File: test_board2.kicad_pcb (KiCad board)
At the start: 2 copper layers, 63.5 x 127 mm, 149 parts, among them P1 MicroB, P2 CONN_01X08, P3 CONN_01X08, P4 CONN_01X10, P5 CONN_01X06, P6 CONN_02X03, Q1 ZXMN2F30FHCT-ND, Q2 Si2305DS, SW1 SWITCH_DPDT, SW2 SW_PUSH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

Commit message: Routing complete, first check. Prior to GND fill.
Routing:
- net LED_PWR_EN: track 113.3 -> 156.0 mm, vias 4 -> 6
- net /*RESET: track 110.6 -> 132.8 mm, vias 4 -> 5
- net VCC: track 248.5 -> 259.2 mm
- net /LED_matrix/LED_3V: track 135.1 -> 144.6 mm
- net (no net): track 4.15 -> 0.00 mm
- net /MOSI: track 121.6 -> 123.2 mm
- net /LED_matrix/DIG0: track 144.0 -> 145.3 mm, vias 20 -> 19
- net I2C_SCL: track 115.4 -> 116.6 mm
- net I2C_SDA: track 97.9 -> 99.1 mm
- net /*IS_USB: track 91.1 -> 92.0 mm
- net /MISO: track 117.9 -> 118.6 mm
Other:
- board text added: "+"
- board text added: "-"

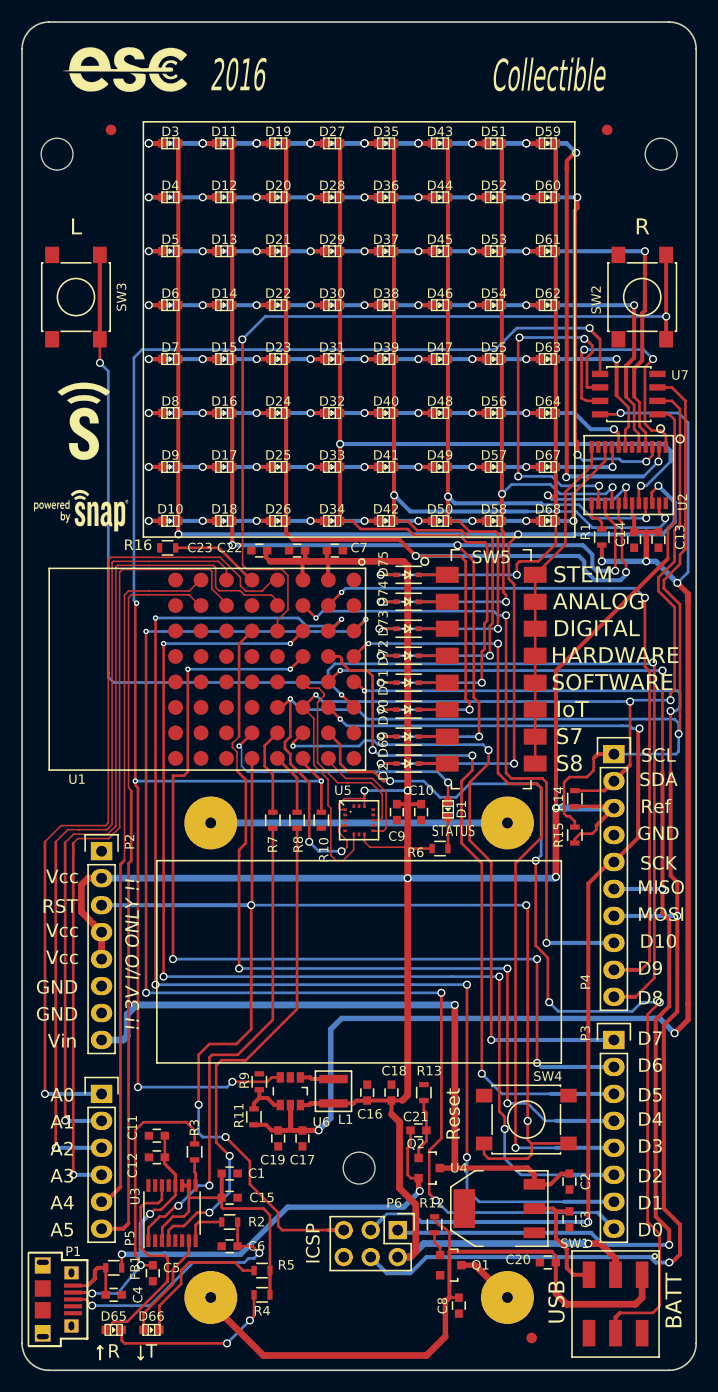
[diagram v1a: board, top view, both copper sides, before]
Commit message: Finished ground pours, all DRC passing
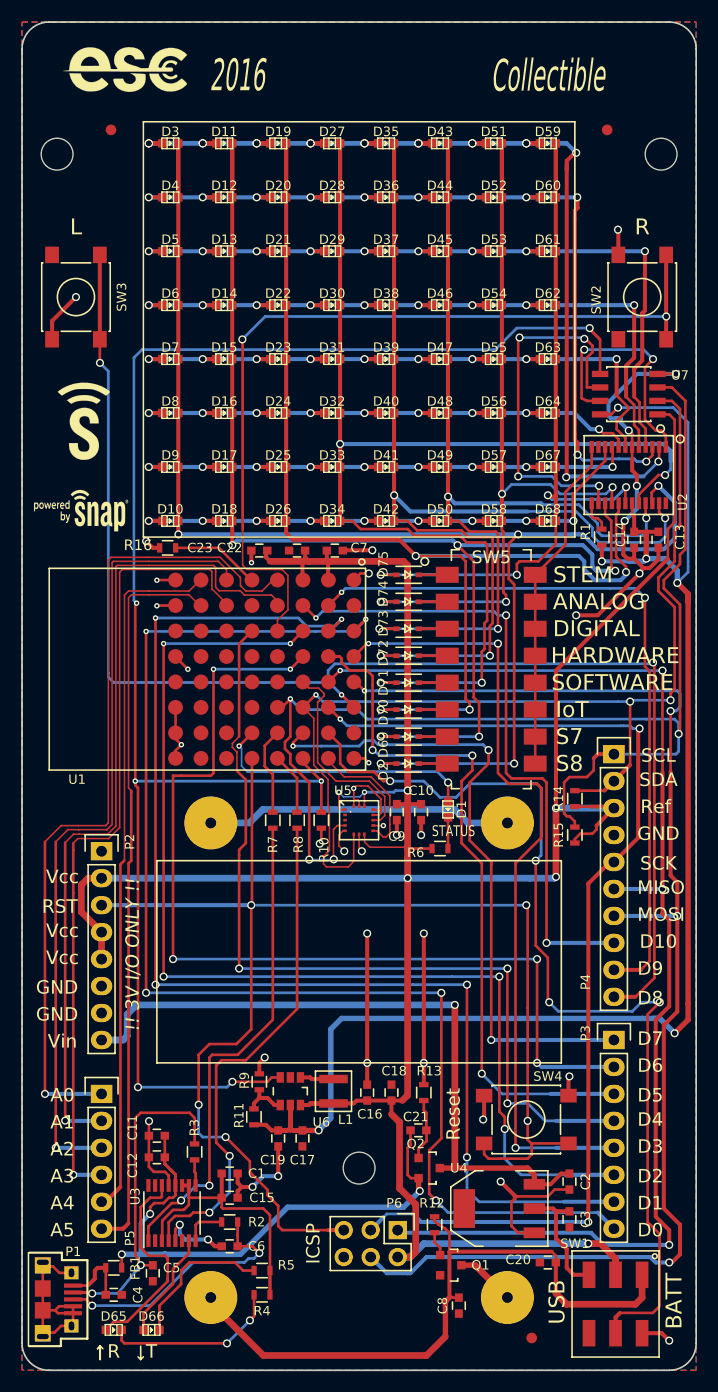
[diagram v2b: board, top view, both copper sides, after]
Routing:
- net GND: track 0.00 -> 178.0 mm, vias 0 -> 38
- net /LED_matrix/SEGE: track 88.6 -> 91.1 mm
- net I2C_SDA: track 99.1 -> 101.6 mm
- net /LED_matrix/SEGD: track 102.6 -> 105.0 mm
- net Net-(C5-Pad1): track 30.6 -> 32.7 mm
- net /LED_matrix/SEGDP: track 131.3 -> 133.4 mm
- net /ACC_INT2: track 11.4 -> 12.6 mm
- net VCC: track 259.2 -> 260.4 mm, vias 6 -> 7
- net I2C_SCL: track 116.6 -> 117.8 mm
- net Net-(BT1-Pad1): track 27.9 -> 29.0 mm
- net /LED_matrix/LED_3V: track 144.6 -> 145.6 mm
- net /LED_matrix/DIG4: track 63.2 -> 63.9 mm
- added copper zone on B.Cu, net GND
- added copper zone on F.Cu, net GND

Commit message: Cleanup, first gerber gen
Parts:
- Fiducial_Mark (x3): footprint Tinkerforge:Fiducial_Mark -> Synapse:Fiducial_Mark
- moved C9 0.08 mm to (178.9, 96.0)
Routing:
- net I2C_SCL: track 117.8 -> 106.8 mm, vias 4 -> 5
- net /LED_matrix/DIG0: track 145.3 -> 134.6 mm
- net /LED_matrix/LED_3V: track 145.6 -> 135.1 mm, vias 6 -> 4
- net /LED_matrix/SEGDP: track 133.4 -> 128.3 mm
- net /LED_matrix/SEGA: track 117.4 -> 112.3 mm
- net /LED_matrix/SEGG: track 73.0 -> 67.9 mm
- net /LED_matrix/SEGF: track 74.7 -> 69.6 mm
- net /LED_matrix/SEGE: track 91.1 -> 86.1 mm
- net /LED_matrix/SEGD: track 105.0 -> 100.0 mm
- net /LED_matrix/SEGC: track 117.6 -> 112.5 mm
- net /LED_matrix/SEGB: track 112.4 -> 107.4 mm
- net GND: track 178.0 -> 182.9 mm, vias 38 -> 39
- net I2C_SDA: track 101.6 -> 98.3 mm, vias 3 -> 2
- net Net-(C5-Pad1): track 32.7 -> 31.1 mm
- net /MOSI: track 123.2 -> 121.7 mm
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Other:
- net class Default: via_drill 0.508 -> 0.3556
- rule pad_to_mask_clearance: 0.2 -> 0.0762
- board text added: "SNAP Badge 2016 REV A"
- board text added: "Synapse Wireless, Inc"

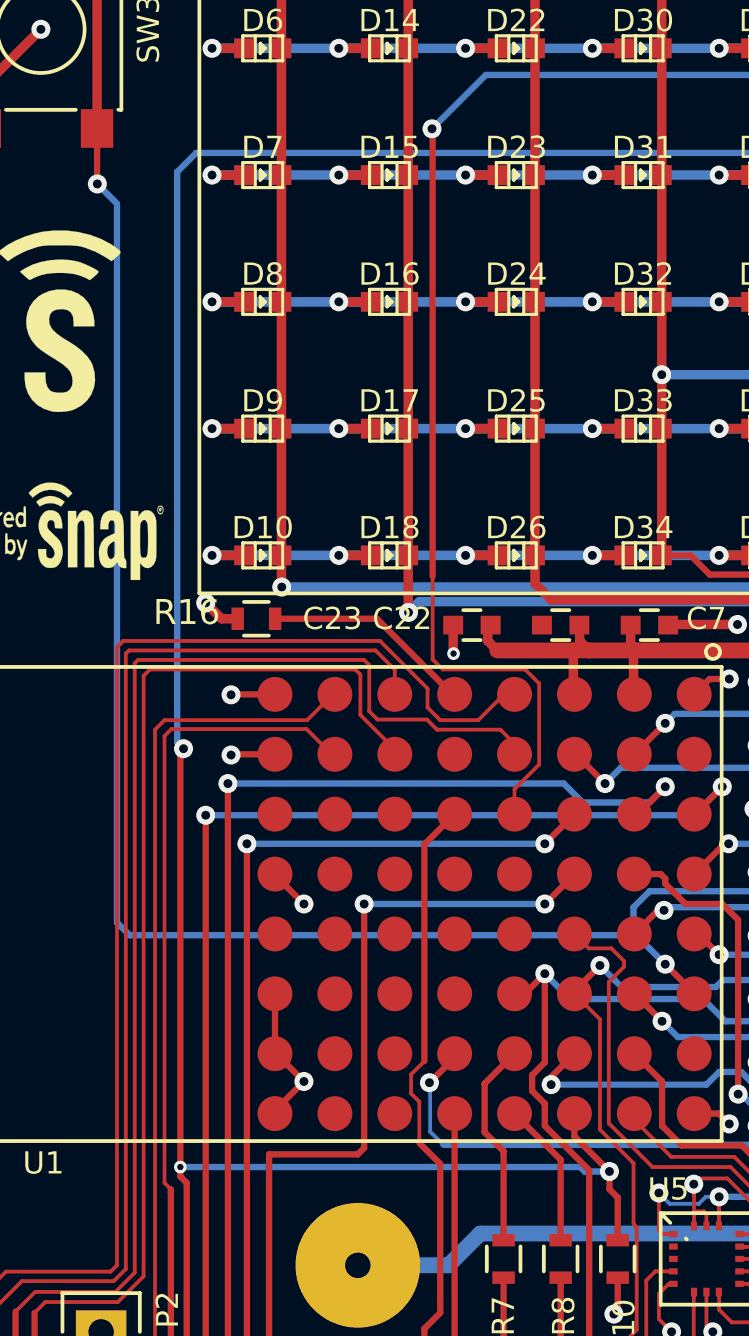
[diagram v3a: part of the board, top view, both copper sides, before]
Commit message: First version sent to CM for review (Screaming Circuits)
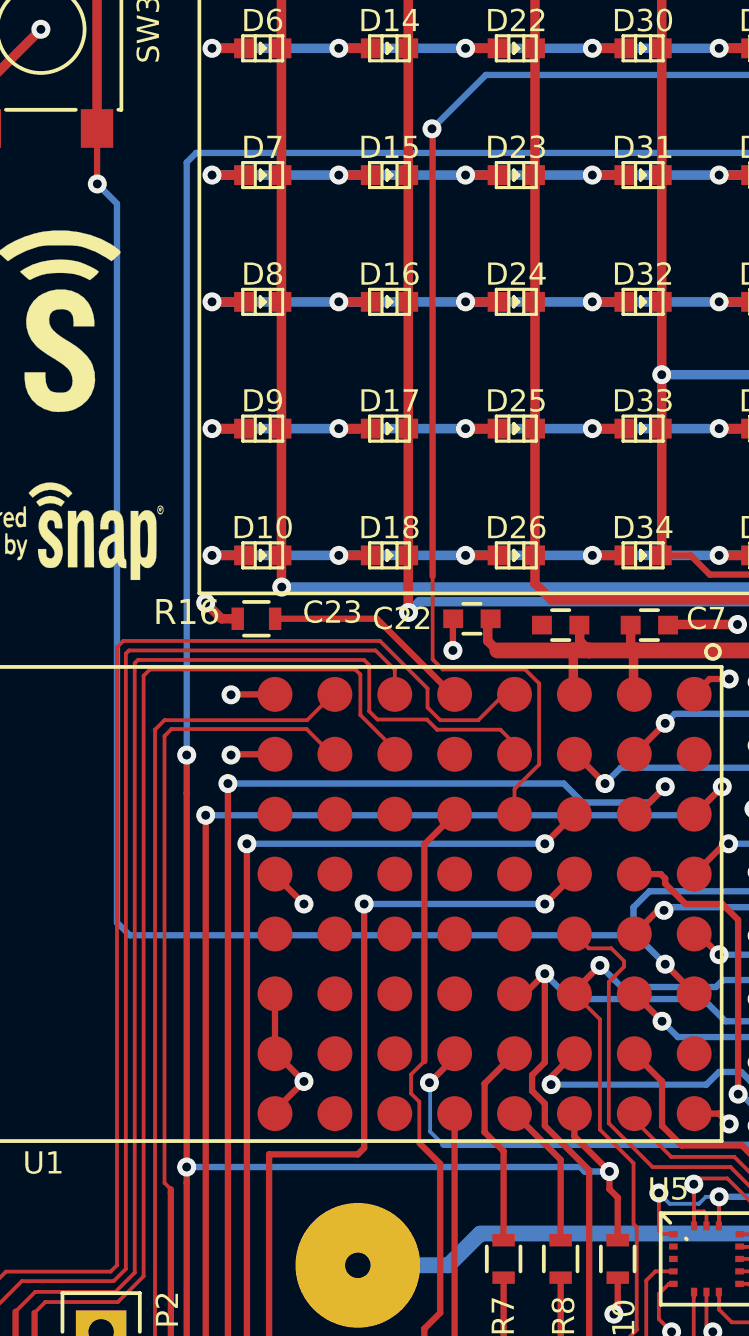
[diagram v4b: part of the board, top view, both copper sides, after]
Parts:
- moved C23 0.25 mm to (165.9, 71.1)
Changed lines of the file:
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@@
     (thickness 1.6)
     (drawings 85)
-    (tracks 1783)
+    (tracks 1782)
     (zones 0)
     (modules 149)
@@
   )
   (setup
-    (last_trace_width 0.1524)
+    (last_trace_width 0.254)
     (user_trace_width 0.1524)
     (user_trace_width 0.254)
@@
   )
   (module Capacitors_SMD:C_0603 (layer F.Cu)
-    (at 165.862 71.374 180)
+    (at 165.862 71.12 180)
     (descr "Capacitor SMD 0603, reflow soldering, AVX (see smccp.pdf)")
     (tags "capacitor 0603")
@@
   (segment (start 169.926 72.39) (end 166.878 72.39) (width 0.635) (layer F.Cu) (net 1))
   (segment (start 179.832 95.262) (end 179.832 93.98) (width 0.635) (layer F.Cu) (net 1))
-  (segment (start 166.497 72.009) (end 166.497 71.489) (width 0.381) (layer F.Cu) (net 1) (status 20))
-  (segment (start 166.497 71.489) (end 166.612 71.374) (width 0.381) (layer F.Cu) (net 1) (status 30))
+  (segment (start 166.497 72.009) (end 166.497 71.235) (width 0.381) (layer F.Cu) (net 1) (status 20))
+  (segment (start 166.497 71.235) (end 166.612 71.12) (width 0.381) (layer F.Cu) (net 1) (status 30))
   (segment (start 181.102 95.262) (end 179.832 95.262) (width 0.381) (layer F.Cu) (net 1) (status 10))
   (segment (start 179.832 95.262) (end 178.8922 95.262) (width 0.381) (layer F.Cu) (net 1) (status 20))
@@
   (segment (start 197.739 68.326) (end 197.358 68.326) (width 0.254) (layer F.Cu) (net 2))
   (segment (start 198.12 68.707) (end 197.739 68.326) (width 0.254) (layer F.Cu) (net 2))
+  (segment (start 165.112 71.12) (end 165.1 71.132) (width 0.254) (layer F.Cu) (net 3))
+  (segment (start 165.1 71.132) (end 165.1 72.39) (width 0.254) (layer F.Cu) (net 3))
+  (via (at 165.1 72.39) (size 0.762) (drill 0.3556) (layers F.Cu B.Cu) (net 3))
   (segment (start 201.676 73.533) (end 204.343 76.2) (width 0.254) (layer B.Cu) (net 3))
   (via (at 201.676 73.533) (size 0.762) (drill 0.3556) (layers F.Cu B.Cu) (net 3))
@@
   (segment (start 173.7494 71.3486) (end 176.5046 71.3486) (width 0.381) (layer F.Cu) (net 3) (status 10))
   (via (at 176.5046 71.3486) (size 0.762) (drill 0.3556) (layers F.Cu B.Cu) (net 3))
-  (segment (start 165.112 71.374) (end 165.112 72.5036) (width 0.381) (layer F.Cu) (net 3) (status 10))
-  (via (at 165.1254 72.517) (size 0.508) (drill 0.254) (layers F.Cu B.Cu) (net 3))
-  (segment (start 165.112 72.5036) (end 165.1254 72.517) (width 0.381) (layer F.Cu) (net 3))
   (segment (start 176.0982 93.5482) (end 174.9806 93.5482) (width 0.1524) (layer F.Cu) (net 3))
   (segment (start 174.9806 93.5482) (end 174.752 93.7768) (width 0.1524) (layer F.Cu) (net 3))
@@
   (segment (start 165.354 123.444) (end 165.354 123.964) (width 0.381) (layer F.Cu) (net 100) (status 20))
   (segment (start 165.862 122.936) (end 165.354 123.444) (width 0.381) (layer F.Cu) (net 100))
+  (segment (start 154.432 78.105) (end 154.432 76.581) (width 0.254) (layer F.Cu) (net 101))
+  (segment (start 154.432 93.091) (end 154.432 78.105) (width 0.254) (layer F.Cu) (net 101))
+  (segment (start 154.432 76.581) (end 154.432 52.832) (width 0.254) (layer B.Cu) (net 101))
+  (via (at 154.432 76.581) (size 0.762) (drill 0.3556) (layers F.Cu B.Cu) (net 101))
+  (segment (start 154.813 52.451) (end 154.432 52.832) (width 0.254) (layer B.Cu) (net 101))
+  (segment (start 154.813 52.451) (end 188.087 52.451) (width 0.254) (layer B.Cu) (net 101))
+  (segment (start 188.087 52.451) (end 190.119 50.419) (width 0.254) (layer B.Cu) (net 101))
+  (segment (start 190.119 50.419) (end 196.977 50.419) (width 0.254) (layer B.Cu) (net 101))
+  (via (at 196.977 50.419) (size 0.762) (drill 0.3556) (layers F.Cu B.Cu) (net 101))
+  (segment (start 196.977 50.419) (end 197.96 51.402) (width 0.1524) (layer F.Cu) (net 101))
+  (segment (start 197.96 51.402) (end 197.96 51.529) (width 0.1524) (layer F.Cu) (net 101))
+  (segment (start 197.96 54.737) (end 197.96 51.529) (width 0.254) (layer F.Cu) (net 101) (status 10))
+  (segment (start 154.432 93.091) (end 154.432 93.726) (width 0.254) (layer F.Cu) (net 101))
+  (segment (start 162.814 121.92) (end 163.322 121.412) (width 0.254) (layer B.Cu) (net 101))
+  (via (at 163.322 121.412) (size 0.762) (drill 0.3556) (layers F.Cu B.Cu) (net 101))
+  (segment (start 163.322 121.412) (end 166.624 121.412) (width 0.254) (layer F.Cu) (net 101))
+  (segment (start 166.624 121.412) (end 167.03548 121.00052) (width 0.254) (layer F.Cu) (net 101))
+  (segment (start 167.03548 121.00052) (end 167.83304 121.00052) (width 0.254) (layer F.Cu) (net 101) (status 20))
+  (via (at 154.432 121.92) (size 0.762) (drill 0.3556) (layers F.Cu B.Cu) (net 101))
+  (segment (start 154.432 93.726) (end 154.432 121.92) (width 0.254) (layer F.Cu) (net 101))
+  (segment (start 154.432 121.92) (end 162.814 121.92) (width 0.254) (layer B.Cu) (net 101))
+  (via (at 154.432 93.091) (size 0.762) (drill 0.3556) (layers F.Cu B.Cu) (net 101))
   (segment (start 169.8498 93.091) (end 170.2054 93.091) (width 0.254) (layer B.Cu) (net 101))
-  (segment (start 154.178 93.091) (end 169.8498 93.091) (width 0.254) (layer B.Cu) (net 101))
-  (via (at 154.178 93.091) (size 0.508) (drill 0.254) (layers F.Cu B.Cu) (net 101))
+  (segment (start 154.178 93.091) (end 154.432 93.091) (width 0.254) (layer B.Cu) (net 101))
+  (segment (start 154.432 93.091) (end 169.8498 93.091) (width 0.254) (layer B.Cu) (net 101))
   (segment (start 170.3832 93.2688) (end 171.3738 93.2688) (width 0.254) (layer B.Cu) (net 101))
   (segment (start 170.2054 93.091) (end 170.3832 93.2688) (width 0.254) (layer B.Cu) (net 101))
@@
   (segment (start 171.5516 93.091) (end 171.3738 93.2688) (width 0.254) (layer B.Cu) (net 101))
   (via (at 171.3738 93.2688) (size 0.762) (drill 0.3556) (layers F.Cu B.Cu) (net 101))
-  (segment (start 154.432 121.92) (end 162.814 121.92) (width 0.254) (layer B.Cu) (net 101))
-  (segment (start 154.178 93.472) (end 154.432 93.726) (width 0.254) (layer F.Cu) (net 101))
-  (segment (start 154.432 93.726) (end 154.432 121.92) (width 0.254) (layer F.Cu) (net 101))
-  (via (at 154.432 121.92) (size 0.762) (drill 0.3556) (layers F.Cu B.Cu) (net 101))
-  (segment (start 154.178 93.091) (end 154.178 93.472) (width 0.254) (layer F.Cu) (net 101))
-  (segment (start 167.03548 121.00052) (end 167.83304 121.00052) (width 0.254) (layer F.Cu) (net 101) (status 20))
-  (segment (start 166.624 121.412) (end 167.03548 121.00052) (width 0.254) (layer F.Cu) (net 101))
-  (segment (start 163.322 121.412) (end 166.624 121.412) (width 0.254) (layer F.Cu) (net 101))
-  (via (at 163.322 121.412) (size 0.762) (drill 0.3556) (layers F.Cu B.Cu) (net 101))
-  (segment (start 162.814 121.92) (end 163.322 121.412) (width 0.254) (layer B.Cu) (net 101))
-  (segment (start 154.051 76.073) (end 154.305 76.327) (width 0.254) (layer B.Cu) (net 101))
-  (segment (start 154.051 76.073) (end 154.051 53.213) (width 0.254) (layer B.Cu) (net 101))
-  (segment (start 154.051 53.213) (end 154.813 52.451) (width 0.254) (layer B.Cu) (net 101))
-  (segment (start 154.813 52.451) (end 188.087 52.451) (width 0.254) (layer B.Cu) (net 101))
-  (segment (start 188.087 52.451) (end 190.119 50.419) (width 0.254) (layer B.Cu) (net 101))
-  (segment (start 190.119 50.419) (end 196.977 50.419) (width 0.254) (layer B.Cu) (net 101))
-  (via (at 196.977 50.419) (size 0.762) (drill 0.3556) (layers F.Cu B.Cu) (net 101))
-  (segment (start 196.977 50.419) (end 197.96 51.402) (width 0.1524) (layer F.Cu) (net 101))
-  (segment (start 197.96 51.402) (end 197.96 51.529) (width 0.1524) (layer F.Cu) (net 101))
-  (segment (start 154.178 76.454) (end 154.178 93.091) (width 0.254) (layer F.Cu) (net 101))
-  (segment (start 154.305 76.327) (end 154.178 76.454) (width 0.254) (layer F.Cu) (net 101))
-  (via (at 154.305 76.327) (size 0.762) (drill 0.3556) (layers F.Cu B.Cu) (net 101))
-  (segment (start 197.96 54.737) (end 197.96 51.529) (width 0.254) (layer F.Cu) (net 101) (status 10))
   (segment (start 167.56888 78.95082) (end 167.56888 77.94752) (width 0.1524) (layer F.Cu) (net 103) (status 10))
   (via (at 204.1906 49.3268) (size 0.762) (drill 0.3556) (layers F.Cu B.Cu) (net 103))

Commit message: Update sch with Mfg and PN fields, added Screaming Circuits to silk.
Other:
- board text added: "Assembled by Screaming Circuits"
- board text added: "PC board by Sunstone Circuits"
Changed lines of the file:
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@@
     (area 143.434999 21.514999 207.085001 148.665001)
     (thickness 1.6)
-    (drawings 85)
+    (drawings 87)
     (tracks 1782)
     (zones 0)
@@
   )
   (layers
-    (0 F.Cu signal)
+    (0 F.Cu signal hide)
     (31 B.Cu signal)
     (32 B.Adhes user)
@@
     (46 B.CrtYd user)
     (47 F.CrtYd user)
-    (48 B.Fab user hide)
+    (48 B.Fab user)
     (49 F.Fab user)
   )
@@
       (clearance 0.65024))
   )
+  (gr_text "Assembled by Screaming Circuits" (at 175.641 83.82) (layer B.SilkS)
+    (effects (font (thickness 0.254) italic) (justify mirror))
+  )
+  (gr_text "PC board by Sunstone Circuits" (at 177.038 80.01) (layer B.SilkS)
+    (effects (font (thickness 0.254) italic) (justify mirror))
+  )
   (gr_text "Synapse Wireless, Inc" (at 175.895 112.776 90) (layer B.SilkS)
